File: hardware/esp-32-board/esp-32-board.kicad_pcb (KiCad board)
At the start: 2 copper layers, 53.8 x 69.1 mm, 34 parts, among them J1 MainConnector, J2 Conn_01x06, J3 ESP-PROG-Program, J4 ESP-PROG-Debug, J5 USB_B_Micro, J6 Barrel_Jack_MountingPin, Q1 BCR129S, SW1 SW_Push, SW2 SW_Push, SW3 SW_DPDT_x2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

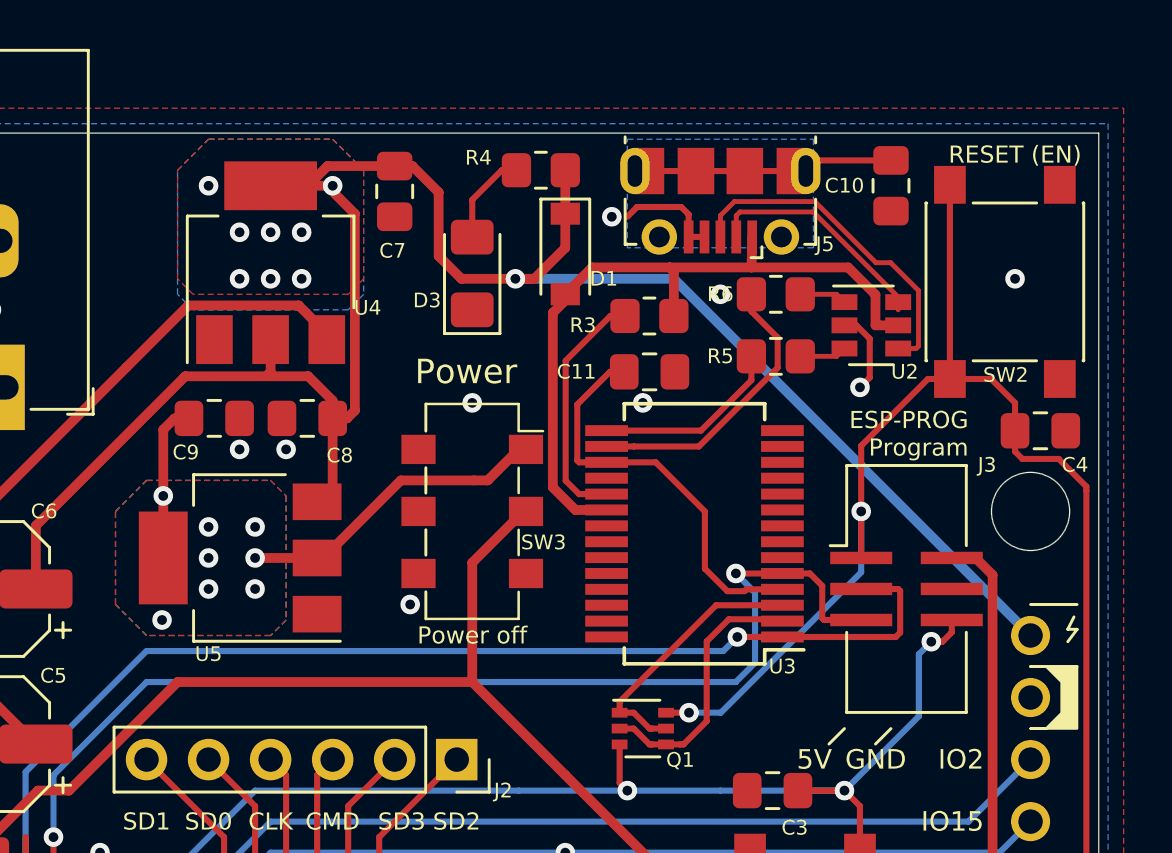
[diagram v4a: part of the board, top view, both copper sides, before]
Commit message: Replace power switch with jumper, add RX/TX leds
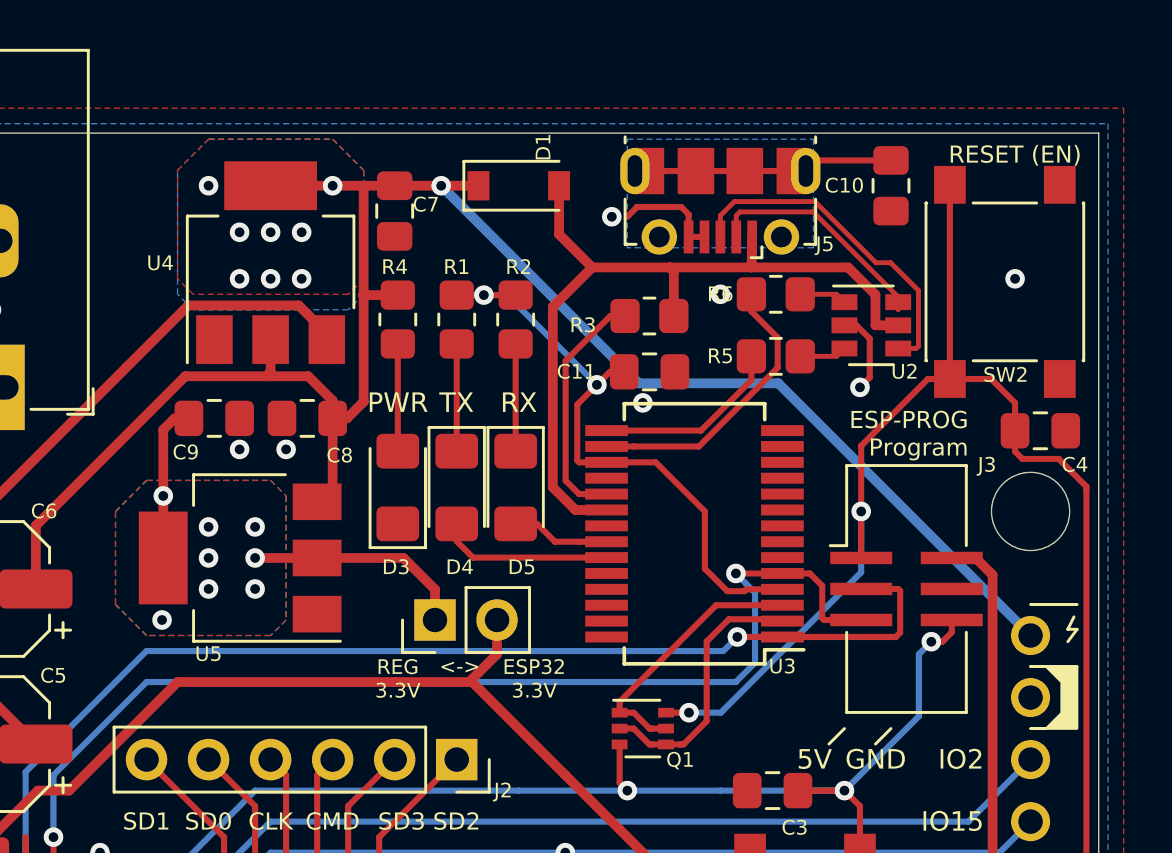
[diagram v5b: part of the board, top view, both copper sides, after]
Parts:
- added D4: RF-GSS150TS-BC, LED_SMD:LED_1206_3216Metric_Pad1.42x1.75mm_HandSolder, F.Cu at (156.8, 35.9)
- added D5: RF-GSS150TS-BC, LED_SMD:LED_1206_3216Metric_Pad1.42x1.75mm_HandSolder, F.Cu at (159.3, 35.9)
- added R1: 220 Ohm, Resistor_SMD:R_0805_2012Metric_Pad1.20x1.40mm_HandSolder, F.Cu at (156.8, 29.0)
- added R2: 220 Ohm, Resistor_SMD:R_0805_2012Metric_Pad1.20x1.40mm_HandSolder, F.Cu at (159.3, 29.0)
- J7: renamed from SW3; value SW_DPDT_x2 -> Conn_01x02; footprint Button_Switch_SMD:Nidec_CL-SB-22B-0X -> Connector_PinHeader_2.54mm:PinHeader_1x02_P2.54mm_Vertical
- moved D3 9.28 mm to (154.4, 35.9)
- moved R4 8.47 mm to (154.4, 29.0), turned to 270 degrees
- moved J7 4.70 mm to (156.0, 41.3), turned to 90 degrees
- moved D1 3.38 mm to (159.4, 23.5), turned to 0 degrees
- moved C7 0.80 mm to (154.3, 24.5)
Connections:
- net Net-(C11-Pad1) renamed /USB/USB_3V3
- U3 pad 22: (no net) -> /USB/RXLED
- U3 pad 23: (no net) -> /USB/TXLED
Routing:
- net /USB/USB_3V3: track 16.8 -> 25.4 mm, vias 0 -> 2
- net +5V: track 84.0 -> 76.2 mm
- net /USB/TXLED: track 0.00 -> 7.12 mm
- net +3V3: track 155.7 -> 150.7 mm
- net Net-(D5-Pad1): track 0.00 -> 4.39 mm
- net Net-(D4-Pad1): track 0.00 -> 4.39 mm
- net /USB/RXLED: track 0.00 -> 4.03 mm
- net /USB/VBUS: track 29.8 -> 33.7 mm
- net /Power/Internal_3V3: track 19.4 -> 15.6 mm
- net Net-(D3-Pad2): track 3.84 -> 4.39 mm
- net GND: vias 16 -> 14
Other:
- board text added: "<->"
- board text added: "ESP32 3.3V"
- board text added: "PWR"
- board text added: "REG 3.3V"
- board text added: "RX"
- board text added: "TX"
- board text removed: "Power"
- board text removed: "Power off"

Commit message: Cleanup tracks and vias
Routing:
- net /TXD0: track 80.4 -> 79.1 mm

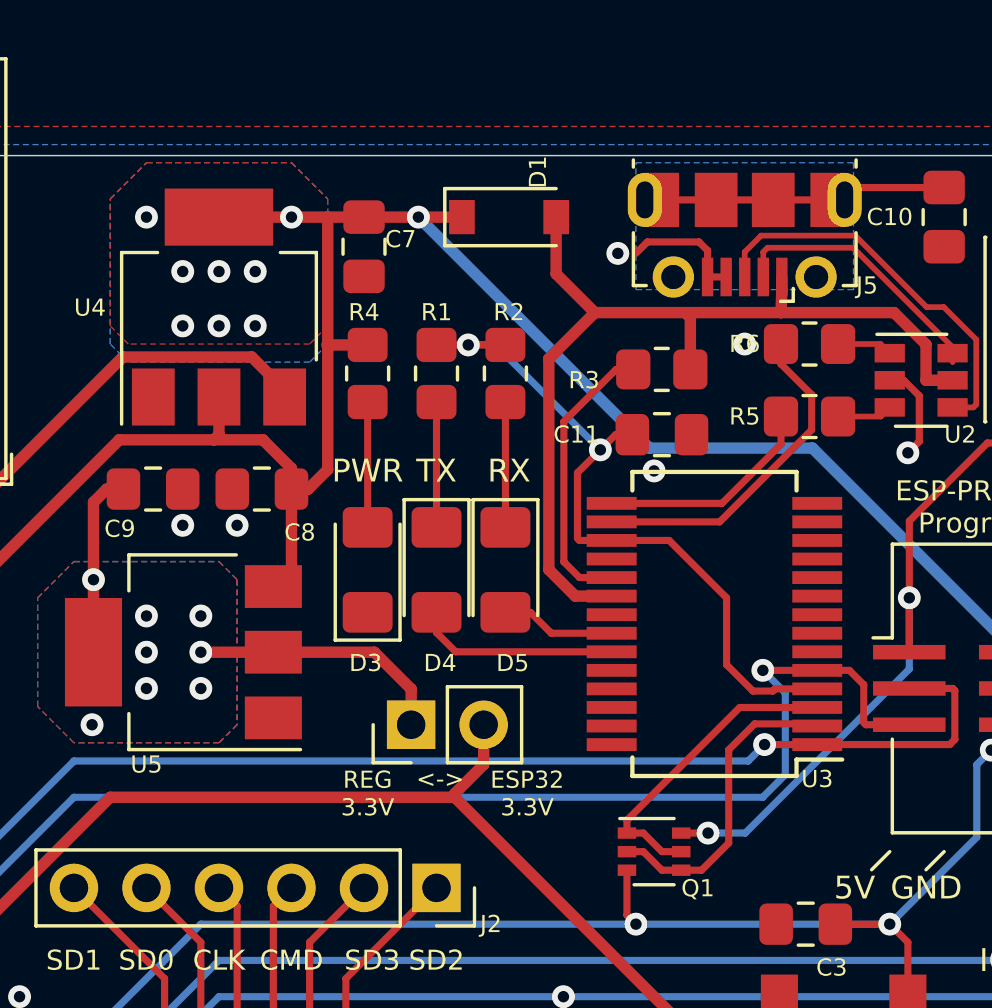
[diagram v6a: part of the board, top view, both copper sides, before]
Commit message: Move LEDs
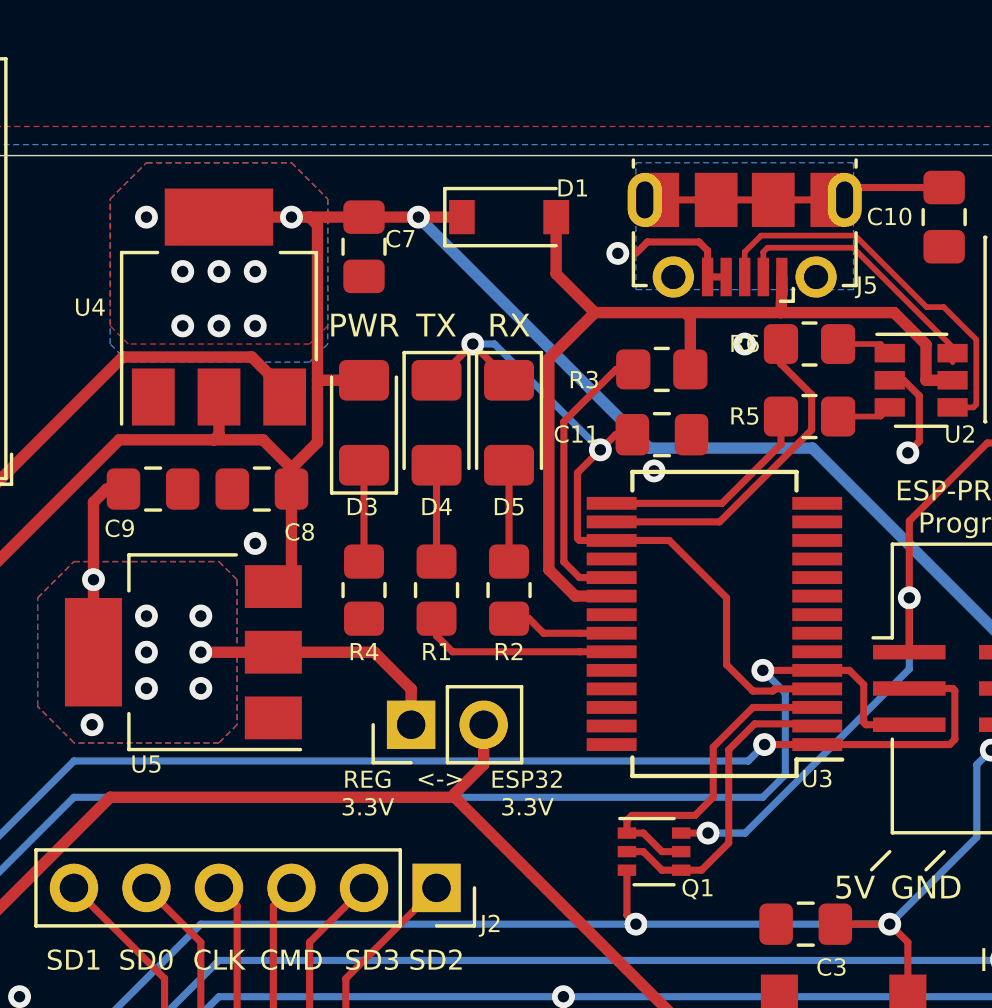
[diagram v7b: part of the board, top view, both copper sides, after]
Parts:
- D4, D5: value RF-GSS150TS-BC -> RF-YUS150TS-AE
- moved R2 7.59 mm to (159.4, 36.6)
- moved R4 7.59 mm to (154.3, 36.6)
- moved R1 7.59 mm to (156.8, 36.6)
- moved D3 5.15 mm to (154.3, 30.7)
- moved D5 5.15 mm to (159.4, 30.7)
- moved D4 5.15 mm to (156.8, 30.7)
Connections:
- D3 pad 1: GND -> Net-(D3-Pad1)
- D3 pad 2: Net-(D3-Pad2) -> +5V
- D4 pad 1: Net-(D4-Pad1) -> /USB/USB_3V3
- D4 pad 2: /USB/TXLED -> Net-(D4-Pad2)
- D5 pad 1: Net-(D5-Pad1) -> /USB/USB_3V3
- D5 pad 2: /USB/RXLED -> Net-(D5-Pad2)
- R1 pad 1: /USB/USB_3V3 -> Net-(D4-Pad2)
- R1 pad 2: Net-(D4-Pad1) -> /USB/TXLED
- R2 pad 1: /USB/USB_3V3 -> Net-(D5-Pad2)
- R2 pad 2: Net-(D5-Pad1) -> /USB/RXLED
- R4 pad 1: +5V -> Net-(D3-Pad1)
- R4 pad 2: Net-(D3-Pad2) -> GND
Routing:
- net Net-(D5-Pad1): track 4.39 -> 0.00 mm
- net Net-(D4-Pad1): track 4.39 -> 0.00 mm
- net Net-(D3-Pad2): track 4.39 -> 0.00 mm
- net Net-(D5-Pad2): track 0.00 -> 3.38 mm
- net Net-(D4-Pad2): track 0.00 -> 3.38 mm
- net Net-(D3-Pad1): track 0.00 -> 3.38 mm
- net /USB/USB_3V3: track 25.4 -> 26.4 mm
- net /USB/RTS: track 10.9 -> 11.9 mm
- net +5V: track 76.2 -> 75.3 mm
- net GND: vias 14 -> 13
